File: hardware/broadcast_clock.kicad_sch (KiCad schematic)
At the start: 1 part

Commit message: Assign footprints
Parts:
- AE1: footprint (none) -> Connector_espena:DC-Power-Jack_DC044_5.5mm_2.1mm
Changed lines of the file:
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@@
       (effects (font (size 1.27 1.27)))
     )
-    (property "Footprint" "" (at 83.82 87.63 0)
+    (property "Footprint" "Connector_espena:DC-Power-Jack_DC044_5.5mm_2.1mm" (at 83.82 87.63 0)
       (effects (font (size 1.27 1.27)) hide)
     )

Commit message: Starting PCB routing process
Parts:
- AE1: footprint Connector_espena:DC-Power-Jack_DC044_5.5mm_2.1mm -> Connector_Coaxial:SMA_Amphenol_132291-12_Vertical
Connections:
- net GND: now also AE1.2 (SHIELD); no longer AE1.1 (SHIELD)
- net GPS timing module/GPS_ANTENNA: now also AE1.1 (ANT); no longer AE1.2 (ANT)
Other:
- sheet MCU ports: added SCL, SDA; removed I2C_SCL, I2C_SDA

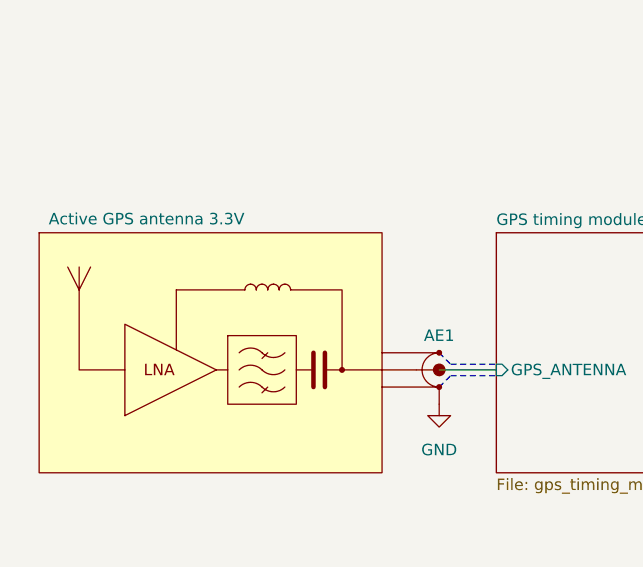
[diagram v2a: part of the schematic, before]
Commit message: Updated project to work with KiCAD version 9
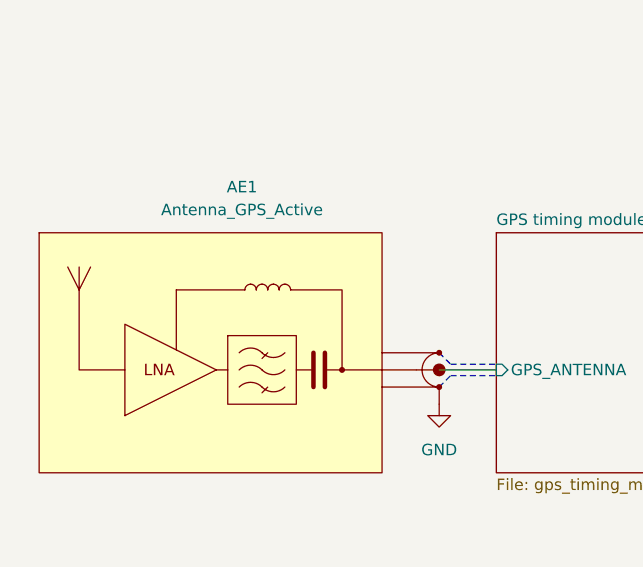
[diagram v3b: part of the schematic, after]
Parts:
- AE1: value Active GPS antenna 3.3V -> Antenna_GPS_Active; footprint Connector_Coaxial:SMA_Amphenol_132291-12_Vertical -> (none)
